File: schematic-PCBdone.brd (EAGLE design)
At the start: 47 x 28 mm, 56 parts, among them J1 FTDI_DEVICERA_SMT, M1 WIRELESS-NRF24L01, Q1 8MHz, T1 NMOS, T2 NMOS, T3 NMOS, T4 NMOS, U1 ATMEGA328P_TQFP, U2 GY-521MPU6050, U3 LTC3534

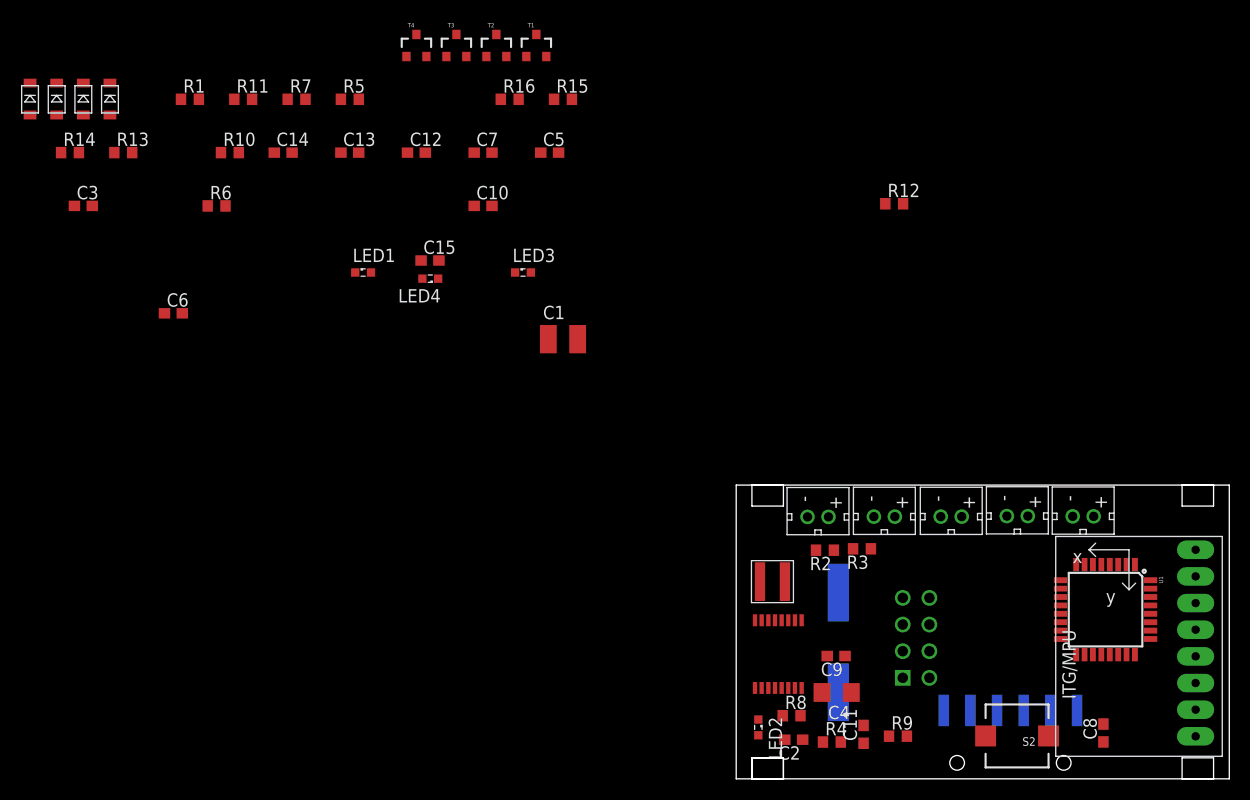
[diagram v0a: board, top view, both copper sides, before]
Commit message: PCB First Draft done
No errors
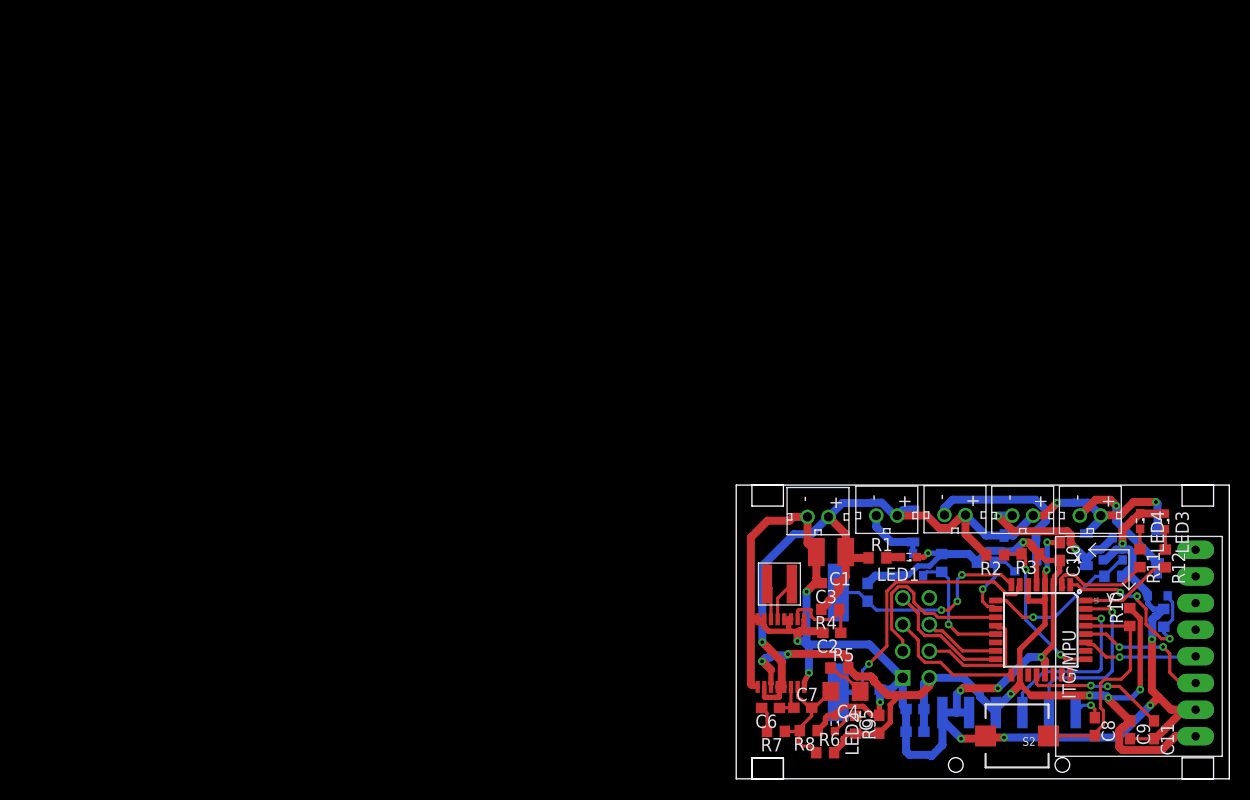
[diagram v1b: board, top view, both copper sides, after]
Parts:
- moved R13 108.6 mm to (40.7, 15.3), flipped to the bottom, turned to 270 degrees
- moved D1 108.6 mm to (40.2, 22.1), flipped to the bottom
- moved R14 107.3 mm to (35.9, 19.3), flipped to the bottom
- moved D2 104.8 mm to (33.4, 21.8), flipped to the bottom
- moved D3 100.8 mm to (27.1, 23.2), flipped to the bottom, turned to 270 degrees
- moved R10 96.5 mm to (37.5, 15.4), turned to 90 degrees
- moved R11 96.0 mm to (38.5, 21.0), turned to 270 degrees
- moved D4 93.5 mm to (16.8, 24.1), flipped to the bottom
- moved C14 81.7 mm to (17.0, 4.50), flipped to the bottom
- moved C3 79.8 mm to (8.97, 18.6), turned to 180 degrees
- moved R1 78.8 mm to (13.5, 21.1)
- moved T1 78.4 mm to (40.2, 18.4), flipped to the bottom
- moved R6 78.0 mm to (8.48, 2.49)
- moved T2 75.9 mm to (35.9, 21.9), flipped to the bottom
- moved R7 75.6 mm to (3.78, 4.52), turned to 180 degrees
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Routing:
- net GND: track 0.00 -> 206.0 mm, vias 0 -> 14
- net V_REG_OUT: track 0.00 -> 110.1 mm, vias 0 -> 8
- net PWR: track 0.00 -> 85.1 mm, vias 0 -> 3
- net N$1: track 0.00 -> 27.0 mm, vias 0 -> 1
- net N$2: track 0.00 -> 21.6 mm
- net N$4: track 0.00 -> 20.2 mm, vias 0 -> 3
- net PWM1: track 0.00 -> 17.9 mm, vias 0 -> 3
- net CE: track 0.00 -> 17.8 mm
- net TXD: track 0.00 -> 17.5 mm, vias 0 -> 1
- net RXD: track 0.00 -> 16.7 mm, vias 0 -> 1
- net N$5: track 0.00 -> 16.5 mm, vias 0 -> 2
- net N$6: track 0.00 -> 16.4 mm
- net V_BAT: track 0.00 -> 15.4 mm, vias 0 -> 2
- net PWM2: track 0.00 -> 15.0 mm, vias 0 -> 1
- net N$25: track 0.00 -> 13.5 mm, vias 0 -> 2
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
